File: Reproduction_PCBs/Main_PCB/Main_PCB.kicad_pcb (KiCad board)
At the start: 4 copper layers, 131.5 x 128 mm, 332 parts, among them CN101 FFC_Conn_01x04, CN102 FFC_Conn_01x12, IC101 CXA1081M, IC102 CXA1082BQ, IC103 RC4558, IC104 BA6290A, IC105 BA6290A, IC106 CXD1167Q, IC107 D4364G, IC108 D78C14GF, IC109 D6378GF, IC201 LC7881M, IC202 RC4560, IC203 RC4558, IC204 RC4558, IC301 L7805, IC302 1951A, P101 Conn_01x10, P102 Conn_01x11, P103 Conn_01x06_Pin, P104 Conn_01x04_Pin, P105 Conn_01x02, P106 Conn_01x02, P107 Conn_01x02, Q101 2SB1132, Q102 DTC114EU3, Q103 2SC2412K, Q104 2SC2412K, Q105 DTC114EU3, Q201 2SC2412K, Q202 2SC2412K, Q203 DTA124EU3, Q204 DTA124EU3, Q205 2SC2412K, Q206 2SC2412K, Q207 DTC114EU3, Q208 2SC2412K, Q209 2SC2412K, Q305 2SC2412K, Q307 2SC2412K, X101 8.4672MHz

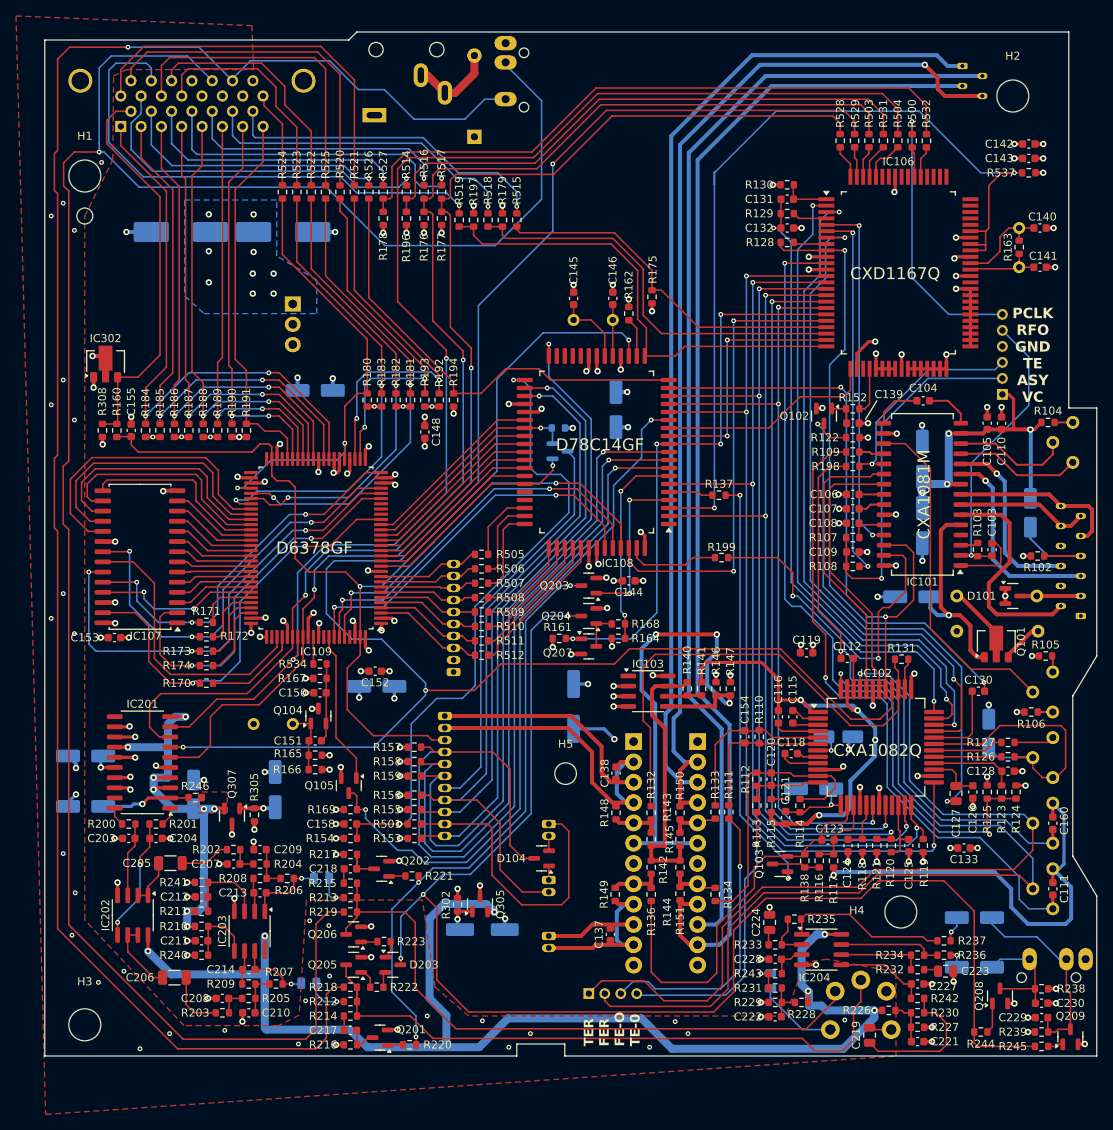
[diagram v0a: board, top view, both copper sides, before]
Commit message: Final fixes to include some ectra mounting holes + GND connection to shield
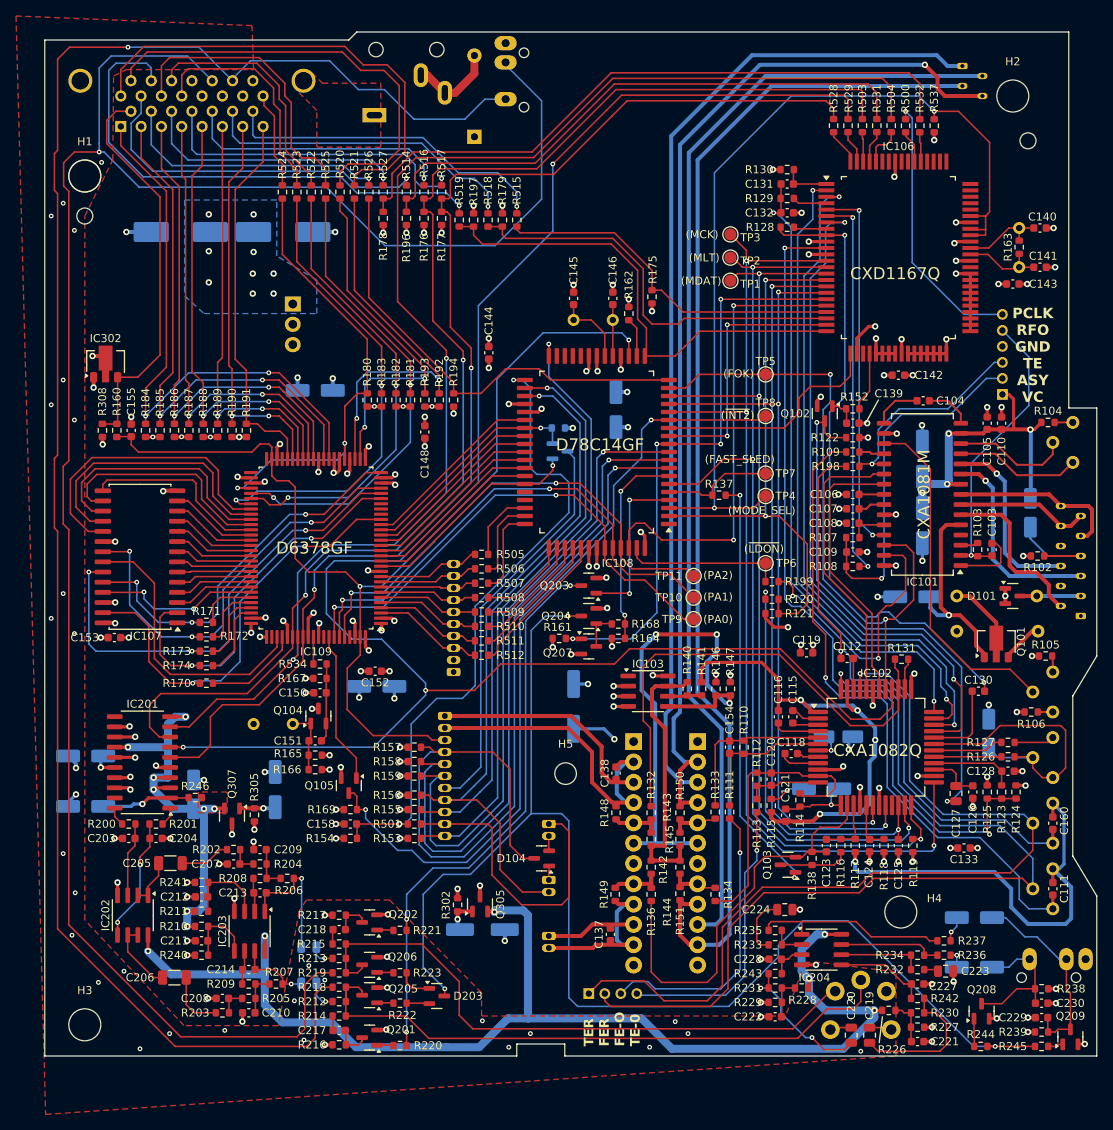
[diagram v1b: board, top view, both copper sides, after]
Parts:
- added TP1: TestPoint, TestPoint:TestPoint_Pad_D1.5mm, F.Cu at (130.7, 109.1)
- added TP10: TestPoint, TestPoint:TestPoint_Pad_D1.5mm, F.Cu at (126.1, 148.7)
- added TP11: TestPoint, TestPoint:TestPoint_Pad_D1.5mm, F.Cu at (126.1, 146.0)
- added TP2: TestPoint, TestPoint:TestPoint_Pad_D1.5mm, F.Cu at (130.7, 106.2)
- added TP3: TestPoint, TestPoint:TestPoint_Pad_D1.5mm, F.Cu at (130.7, 103.3)
- added TP4: TestPoint, TestPoint:TestPoint_Pad_D1.5mm, F.Cu at (135.1, 136.0)
- added TP5: TestPoint, TestPoint:TestPoint_Pad_D1.5mm, F.Cu at (135.1, 120.8)
- added TP6: TestPoint, TestPoint:TestPoint_Pad_D1.5mm, F.Cu at (135.1, 144.4)
- added TP7: TestPoint, TestPoint:TestPoint_Pad_D1.5mm, F.Cu at (135.1, 133.2)
- added TP8: TestPoint, TestPoint:TestPoint_Pad_D1.5mm, F.Cu at (135.1, 126.0)
- added TP9: TestPoint, TestPoint:TestPoint_Pad_D1.5mm, F.Cu at (126.1, 151.4)
- C220: moved to F.Cu
- H1, H2, H3, H4: value MountingHole -> MountingHole_4mm; footprint MountingHole:MountingHole_4mm -> PC-Engine_CDR-30A:MountingHole_4mm
- H5: value MountingHole -> MountingHole_2.7mm; footprint MountingHole:MountingHole_2.7mm -> PC-Engine_CDR-30A:MountingHole_2.7mm
- moved R120 34.2 mm to (135.9, 148.9), turned to 180 degrees
- moved C144 33.4 mm to (100.5, 118.1), turned to -90 degrees
- moved C142 33.2 mm to (151.7, 120.9)
- moved R121 31.8 mm to (135.9, 150.7), turned to 180 degrees
- moved C143 15.8 mm to (166.0, 109.5)
- moved R537 13.2 mm to (156.2, 89.7), turned to 90 degrees
- moved C220 12.2 mm to (145.8, 203.4), turned to 90 degrees
- moved C216 8.75 mm to (78.0, 192.4)
- moved R213 7.73 mm to (81.8, 193.8)
- moved C218 7.73 mm to (81.8, 190.2)
- moved R215 7.73 mm to (81.8, 192.0)
- moved R217 7.73 mm to (81.8, 188.4)
- moved R219 7.73 mm to (81.8, 195.6)
- moved R199 6.98 mm to (135.9, 146.7)
- moved R221 6.96 mm to (89.4, 190.3)
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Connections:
- net Net-(IC108-PC3/~{INT2}) renamed /MCU/~{INT2}
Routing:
- net Net-(IC102-XRST): track 8.95 -> 50.6 mm, vias 0 -> 2
- net /XRST: track 103.9 -> 69.2 mm, vias 3 -> 2
- net +9VA: track 170.4 -> 153.7 mm
- net /PA0: track 47.6 -> 63.3 mm
- net Net-(C220-Pad1): track 4.02 -> 18.6 mm, vias 1 -> 2
- net Net-(D203-A): track 175.0 -> 161.0 mm
- net /PA1: track 49.1 -> 62.6 mm
- net Net-(JK104D-~{SCSI_REQ}): track 43.6 -> 55.9 mm
- net /MCU/~{INT2}: track 87.0 -> 99.3 mm
- net /PA2: track 50.4 -> 61.7 mm
- net Net-(JK104C-~{SCSI_ACK}): track 48.6 -> 59.2 mm
- net /AUDIO/LINEOUT_R: track 264.8 -> 255.6 mm
- net Net-(IC101-~{LDON}): track 42.9 -> 34.2 mm
- net /FAST_SLED: track 5.58 -> 14.0 mm
- net /~{LDON}: track 11.7 -> 19.9 mm
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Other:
- outline, holes or cut-outs redrawn
- board text added: "(FAST_SLED)"
- board text added: "(FOK)"
- board text added: "(MCK)"
- board text added: "(MDAT)"
- board text added: "(MLT)"
- board text added: "(MODE_SEL)"
- board text added: "(PA0)"
- board text added: "(PA1)"
- board text added: "(PA2)"
- board text added: "(~{INT2})"
- board text added: "(~{LDON})"

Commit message: Final commit before ordering
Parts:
- removed R534: 0, Resistor_SMD:R_0603_1608Metric
- C102: footprint Capacitor_SMD:CP_Elec_4x5.4 -> Capacitor_SMD:C_0805_2012Metric; moved to F.Cu
- C117: footprint Capacitor_SMD:CP_Elec_4x5.4 -> Capacitor_SMD:C_0805_2012Metric
- IC107: footprint Package_SO:SOIC-28W_7.5x17.9mm_P1.27mm -> Package_SO:SOP-28_8.4x18.16mm_P1.27mm
- moved C127 48.6 mm to (142.4, 127.5), turned to 0 degrees
- moved R108 27.7 mm to (160.8, 121.4), turned to 180 degrees
- moved C109 24.7 mm to (160.8, 123.2), turned to 0 degrees
- moved R532 17.4 mm to (137.8, 84.4), turned to 0 degrees
- moved C113 16.8 mm to (152.0, 148.0), turned to 0 degrees
- moved R500 14.3 mm to (164.8, 97.1), turned to 180 degrees
- moved R504 13.5 mm to (137.8, 86.2), turned to 180 degrees
- moved R537 12.5 mm to (164.8, 98.8), turned to 180 degrees
- moved C101 12.2 mm to (161.2, 139.1), turned to 180 degrees
- moved R531 11.3 mm to (137.8, 88.0), turned to 0 degrees
- moved R503 9.40 mm to (137.8, 89.8), turned to 180 degrees
- moved R102 9.00 mm to (169.3, 134.5), turned to -90 degrees
- moved R529 7.83 mm to (137.8, 91.6), turned to 0 degrees
- moved R528 6.88 mm to (137.8, 93.4), turned to 0 degrees
- moved Q101 4.60 mm to (163.9, 149.6)
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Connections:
- C150 pad 2: Net-(Q104-E) -> Net-(IC109-XIN)
- C151 pad 1: Net-(Q104-E) -> Net-(IC109-XIN)
- Q104 pad 2: Net-(Q104-E) -> Net-(IC109-XIN)
- R167 pad 2: Net-(Q104-E) -> Net-(IC109-XIN)
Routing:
- net Net-(Q102-C): track 66.6 -> 5.29 mm, vias 2 -> 0
- net /VC: track 165.3 -> 109.8 mm, vias 11 -> 13
- net Net-(IC102-BW): track 6.12 -> 58.8 mm, vias 0 -> 2
- net GND: track 206.3 -> 241.9 mm
- net /SFSY: track 81.9 -> 59.0 mm
- net /~{I2S_SCLK}: track 169.1 -> 147.3 mm
- net /MODE_SELECT: track 113.9 -> 95.1 mm
- net /DSP/ASY: track 48.8 -> 30.3 mm
- net Net-(IC106-DA08): track 3.71 -> 21.3 mm
- net /I2S_DAT: track 164.8 -> 147.5 mm
- net /I2S_SCLK: track 71.8 -> 54.5 mm
- net /I2S_WDLK: track 235.0 -> 219.2 mm
- net /I2S_LRCK: track 154.2 -> 141.8 mm
- net Net-(IC106-DA09): track 4.11 -> 14.3 mm
- net Net-(Q104-E): track 9.87 -> 0.00 mm
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- added copper zone on B.Cu, net +5V
- added copper zone on B.Cu, net /VC
